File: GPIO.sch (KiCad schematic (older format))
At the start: 13 parts, among them P1 CONN_12, SW1 SW_PUSH_SMALL, SW2 SW_PUSH_SMALL, SW3 SW_PUSH_SMALL

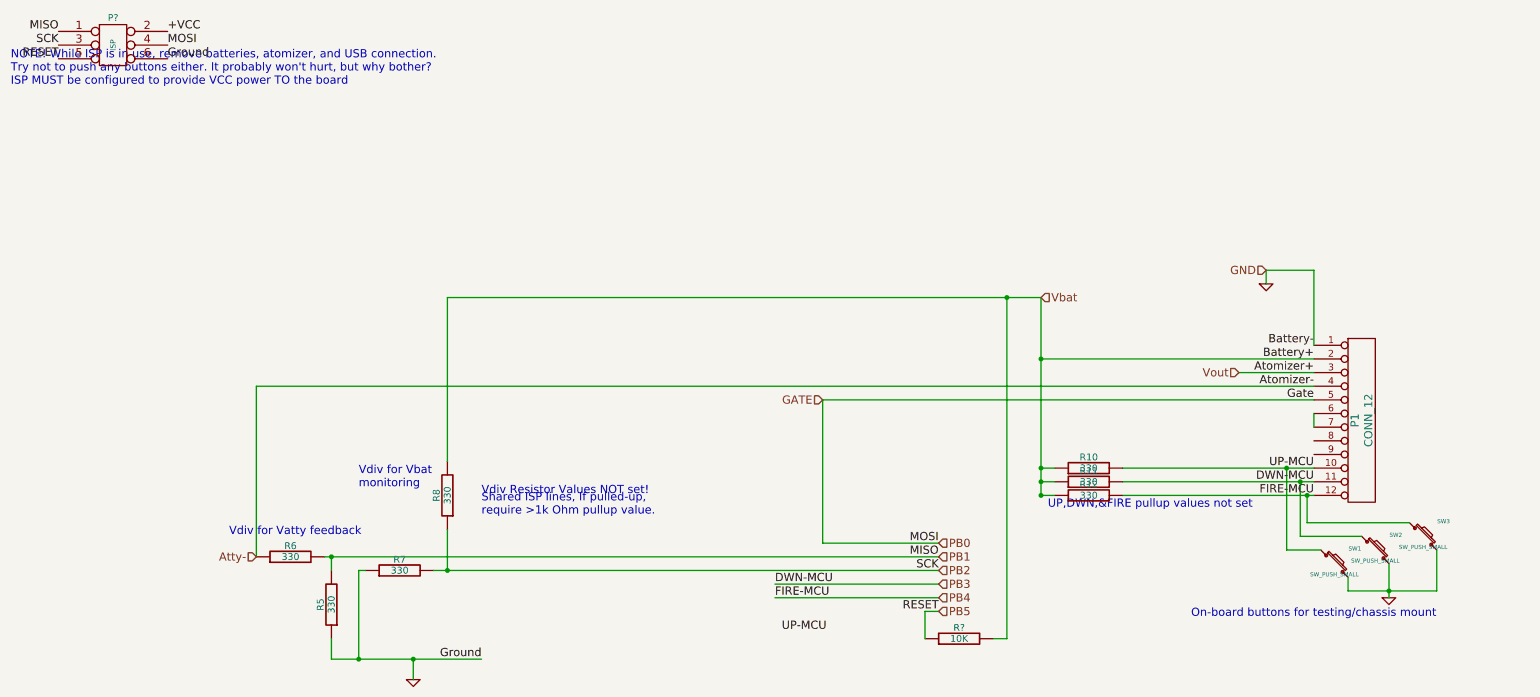
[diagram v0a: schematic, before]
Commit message: Another boost circuit, alpha ready
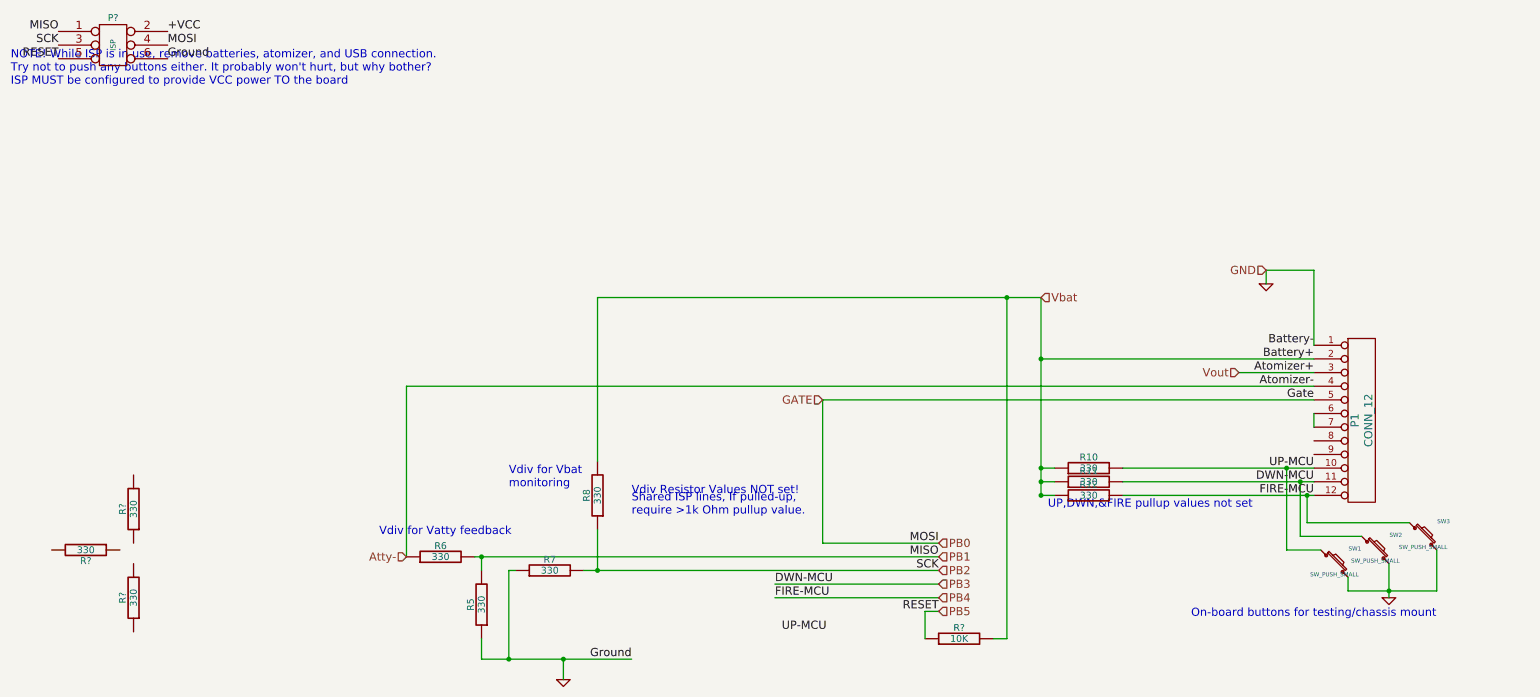
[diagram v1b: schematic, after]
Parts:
- added R? (x3): 330, symbol R
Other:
- moved on the sheet: R5, R6, R7, R8
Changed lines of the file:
@@
-EESchema Schematic File Version 2  date Sat 06 Apr 2013 02:34:34 AM CDT
+EESchema Schematic File Version 2  date Sat 06 Apr 2013 08:45:37 PM CDT
 LIBS:power
 LIBS:device
@@
 Sheet 4 4
 Title ""
-Date "6 apr 2013"
+Date "7 apr 2013"
 Rev ""
 Comp ""
@@
 L GND #PWR04
 U 1 1 5155BA90
-P 3450 5450
-F 0 "#PWR04" H 3450 5450 30  0001 C CNN
-F 1 "GND" H 3450 5380 30  0001 C CNN
-F 2 "" H 3450 5450 60  0001 C CNN
-F 3 "" H 3450 5450 60  0001 C CNN
-	1    3450 5450
+P 4550 5450
+F 0 "#PWR04" H 4550 5450 30  0001 C CNN
+F 1 "GND" H 4550 5380 30  0001 C CNN
+F 2 "" H 4550 5450 60  0001 C CNN
+F 3 "" H 4550 5450 60  0001 C CNN
+	1    4550 5450
 	1    0    0    -1
 $EndComp
@@
 L R R8
 U 1 1 5155BB33
-P 3700 4100
-F 0 "R8" V 3780 4100 50  0000 C CNN
-F 1 "330" V 3700 4100 50  0000 C CNN
-F 2 "" H 3700 4100 60  0001 C CNN
-F 3 "" H 3700 4100 60  0001 C CNN
-	1    3700 4100
+P 4800 4100
+F 0 "R8" V 4880 4100 50  0000 C CNN
+F 1 "330" V 4800 4100 50  0000 C CNN
+F 2 "" H 4800 4100 60  0001 C CNN
+F 3 "" H 4800 4100 60  0001 C CNN
+	1    4800 4100
 	-1   0    0    1
 $EndComp
@@
 L R R7
 U 1 1 5155BB45
-P 3350 4650
-F 0 "R7" V 3430 4650 50  0000 C CNN
-F 1 "330" V 3350 4650 50  0000 C CNN
-F 2 "" H 3350 4650 60  0001 C CNN
-F 3 "" H 3350 4650 60  0001 C CNN
-	1    3350 4650
-	0    -1   -1   0
-$EndComp
-Text Notes 3050 4050 0    60   ~ 0
+P 4450 4650
+F 0 "R7" V 4530 4650 50  0000 C CNN
+F 1 "330" V 4450 4650 50  0000 C CNN
+F 2 "" H 4450 4650 60  0001 C CNN
+F 3 "" H 4450 4650 60  0001 C CNN
+	1    4450 4650
+	0    -1   -1   0
+$EndComp
+Text Notes 4150 4050 0    60   ~ 0
 Vdiv for Vbat\nmonitoring
 $Comp
 L R R6
 U 1 1 5155BC78
-P 2550 4550
-F 0 "R6" V 2630 4550 50  0000 C CNN
-F 1 "330" V 2550 4550 50  0000 C CNN
-F 2 "" H 2550 4550 60  0001 C CNN
-F 3 "" H 2550 4550 60  0001 C CNN
-	1    2550 4550
-	0    -1   -1   0
-$EndComp
-Text Notes 2100 4400 0    60   ~ 0
+P 3650 4550
+F 0 "R6" V 3730 4550 50  0000 C CNN
+F 1 "330" V 3650 4550 50  0000 C CNN
+F 2 "" H 3650 4550 60  0001 C CNN
+F 3 "" H 3650 4550 60  0001 C CNN
+	1    3650 4550
+	0    -1   -1   0
+$EndComp
+Text Notes 3200 4400 0    60   ~ 0
 Vdiv for Vatty feedback
 $Comp
 L R R5
 U 1 1 5155C2FA
-P 2850 4900
-F 0 "R5" V 2930 4900 50  0000 C CNN
-F 1 "330" V 2850 4900 50  0000 C CNN
-F 2 "" H 2850 4900 60  0001 C CNN
-F 3 "" H 2850 4900 60  0001 C CNN
-	1    2850 4900
+P 3950 4900
+F 0 "R5" V 4030 4900 50  0000 C CNN
+F 1 "330" V 3950 4900 50  0000 C CNN
+F 2 "" H 3950 4900 60  0001 C CNN
+F 3 "" H 3950 4900 60  0001 C CNN
+	1    3950 4900
 	-1   0    0    1
 $EndComp
@@
 Text Label 1650 900  0    60   ~ 0
 Ground
-Text Label 3950 5300 2    60   ~ 0
+Text Label 5050 5300 2    60   ~ 0
 Ground
 Text Label 7300 4450 2    60   ~ 0
@@
 Text Notes 500  1100 0    60   ~ 0
 NOTE! While ISP is in use, remove batteries, atomizer, and USB connection.\nTry not to push any buttons either. It probably won't hurt, but why bother?\nISP MUST be configured to provide VCC power TO the board
-Text Notes 3950 4100 0    60   ~ 0
+Text Notes 5050 4100 0    60   ~ 0
 Vdiv Resistor Values NOT set!
 Text HLabel 8050 2650 2    60   Input ~ 0
@@
 	9700 2450 9700 2550
 Wire Wire Line
-	3450 5300 3450 5450
-Wire Wire Line
-	2850 5300 3050 5300
-Wire Wire Line
-	3050 5300 3450 5300
-Wire Wire Line
-	3450 5300 3950 5300
-Connection ~ 3450 5300
-Wire Wire Line
-	3700 4350 3700 4650
-Wire Wire Line
-	2800 4550 2850 4550
-Wire Wire Line
-	2850 4550 7300 4550
-Wire Wire Line
-	2850 5150 2850 5300
-Wire Wire Line
-	3600 4650 3700 4650
-Wire Wire Line
-	3700 4650 7300 4650
-Connection ~ 3700 4650
+	4550 5300 4550 5450
+Wire Wire Line
+	3950 5300 4150 5300
+Wire Wire Line
+	4150 5300 4550 5300
+Wire Wire Line
+	4550 5300 5050 5300
+Connection ~ 4550 5300
+Wire Wire Line
+	4800 4350 4800 4650
+Wire Wire Line
+	3900 4550 3950 4550
+Wire Wire Line
+	3950 4550 7300 4550
+Wire Wire Line
+	3950 5150 3950 5300
+Wire Wire Line
+	4700 4650 4800 4650
+Wire Wire Line
+	4800 4650 7300 4650
+Connection ~ 4800 4650
 Wire Wire Line
 	8650 4100 10000 4100
@@
 	10000 4100 10050 4100
 Wire Wire Line
-	3100 4650 3050 4650
-Wire Wire Line
-	3050 4650 3050 5300
-Connection ~ 3050 5300
+	4200 4650 4150 4650
+Wire Wire Line
+	4150 4650 4150 5300
+Connection ~ 4150 5300
 Wire Wire Line
 	8050 4100 8150 4100
@@
 	10950 4800 10950 4500
 Wire Wire Line
-	2850 4550 2850 4650
-Connection ~ 2850 4550
+	3950 4550 3950 4650
+Connection ~ 3950 4550
 Wire Wire Line
 	10050 2450 9700 2450
@@
 	10050 3500 10050 3600
 Wire Wire Line
-	3700 2650 3700 3850
-Wire Wire Line
-	3700 2650 7800 2650
+	4800 2650 4800 3850
+Wire Wire Line
+	4800 2650 7800 2650
 Wire Wire Line
 	7800 2650 8050 2650
@@
 Text HLabel 9700 2450 0    60   Input ~ 0
 GND
-Text Notes 3950 4250 0    60   ~ 0
+Text Notes 5050 4250 0    60   ~ 0
 Shared ISP lines, If pulled-up, \nrequire >1k Ohm pullup value.
 Wire Wire Line
-	10050 3300 2300 3300
-Wire Wire Line
-	2300 3300 2300 4550
+	10050 3300 3400 3300
+Wire Wire Line
+	3400 3300 3400 4550
 Text HLabel 6450 3400 0    60   Input ~ 0
 GATE
-Text HLabel 2300 4550 0    60   Input ~ 0
+Text HLabel 3400 4550 0    60   Input ~ 0
 Atty-
+$Comp
+L R R?
+U 1 1 5160CCB0
+P 1400 4200
+F 0 "R?" V 1480 4200 50  0000 C CNN
+F 1 "330" V 1400 4200 50  0000 C CNN
+F 2 "" H 1400 4200 60  0001 C CNN
+F 3 "" H 1400 4200 60  0001 C CNN
+	1    1400 4200
+	-1   0    0    1
+$EndComp
+$Comp
+L R R?
+U 1 1 5160CCD1
+P 1400 4850
+F 0 "R?" V 1480 4850 50  0000 C CNN
+F 1 "330" V 1400 4850 50  0000 C CNN
+F 2 "" H 1400 4850 60  0001 C CNN
+F 3 "" H 1400 4850 60  0001 C CNN
+	1    1400 4850
+	-1   0    0    1
+$EndComp
+$Comp
+L R R?
+U 1 1 5160CCD8
+P 1050 4500
+F 0 "R?" V 1130 4500 50  0000 C CNN
+F 1 "330" V 1050 4500 50  0000 C CNN
+F 2 "" H 1050 4500 60  0001 C CNN
+F 3 "" H 1050 4500 60  0001 C CNN
+	1    1050 4500
+	0    1    1    0
+$EndComp
 $EndSCHEMATC
